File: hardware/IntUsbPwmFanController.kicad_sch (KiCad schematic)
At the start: 53 parts, among them J1 UsbPortA, J2 UsbPortB, J3 MOLEX, J6 FAN, J7 USB_Out, J8 GPIO, Q1 IRLML6402, U1 FT260S, U2 AT24CS01-SSHM, U3 ATtiny202-SS

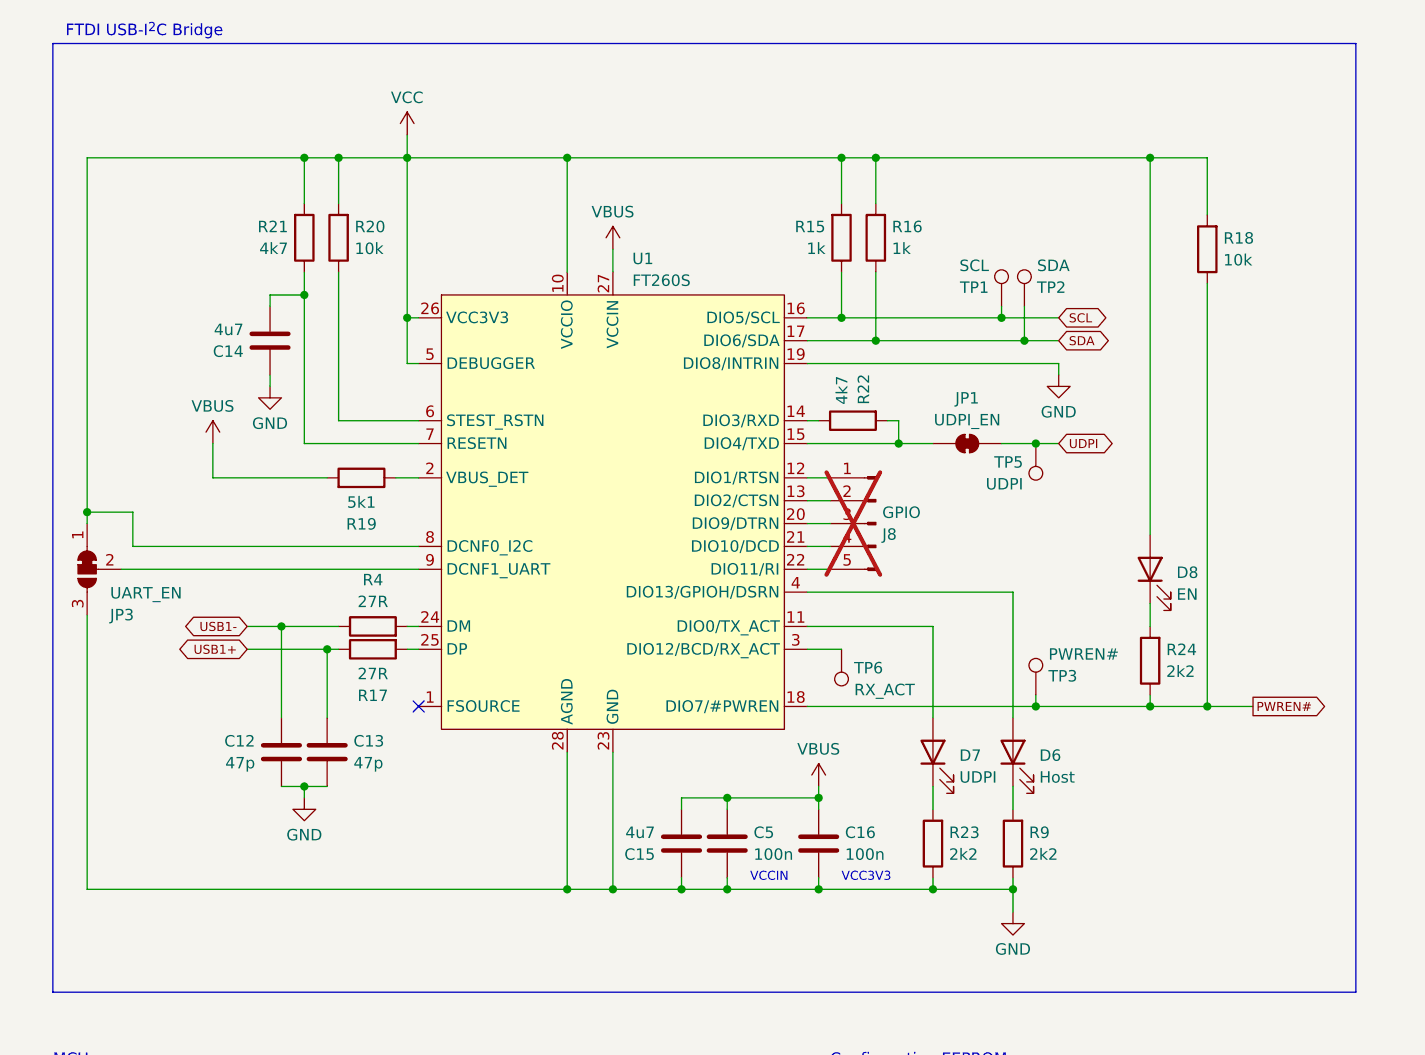
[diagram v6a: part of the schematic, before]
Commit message: Fix FT260S decoupling cap assignment
C16 was accidentally assigned to vbus, when it should have been VCC3V3.
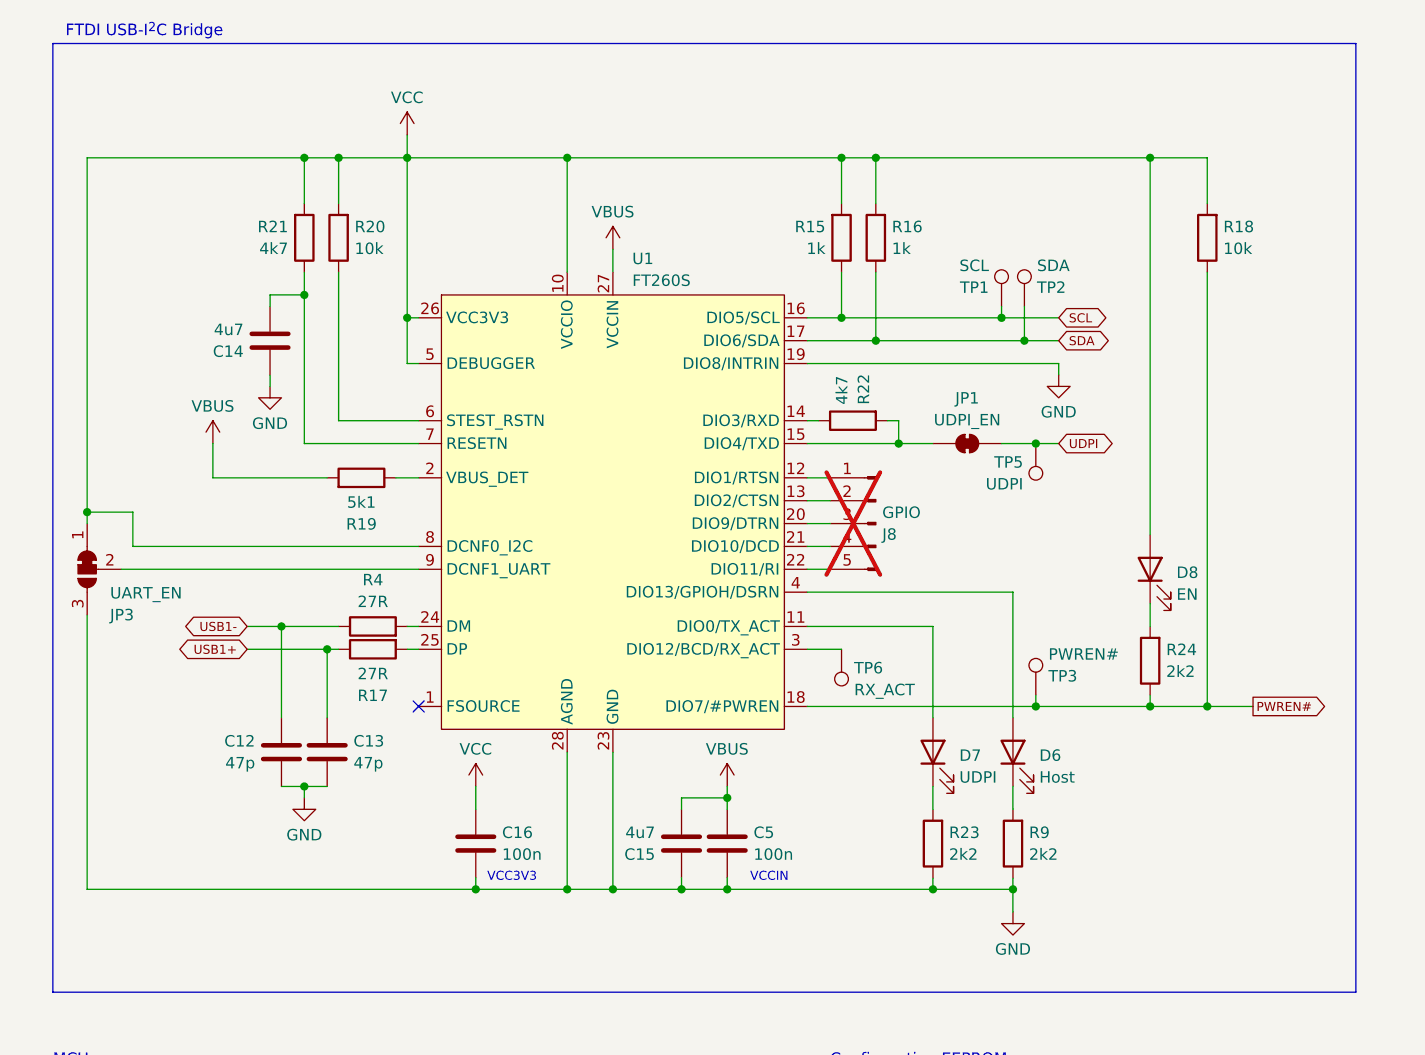
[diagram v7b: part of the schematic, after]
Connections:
- net VBUS: no longer C16.1
- net VCC: now also C16.1
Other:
- moved on the sheet: C16, R18
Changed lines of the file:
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@@
 	(text "VCC3V3"
 		(exclude_from_sim no)
-		(at 106.68 110.49 0)
+		(at 67.31 110.49 0)
 		(effects
 			(font
@@
 	)
 	(junction
+		(at 66.04 111.76)
+		(diameter 0)
+		(color 0 0 0 0)
+	)
+	(junction
 		(at 93.98 101.6)
 		(diameter 0)
@@
 	)
 	(junction
-		(at 104.14 111.76)
-		(diameter 0)
-		(color 0 0 0 0)
-	)
-	(junction
 		(at 212.09 96.52)
 		(diameter 0)
@@
 	)
 	(junction
-		(at 104.14 101.6)
-		(diameter 0)
-		(color 0 0 0 0)
-	)
-	(junction
 		(at 196.85 96.52)
 		(diameter 0)
@@
 	(wire
 		(pts
-			(xy 147.32 30.48) (xy 147.32 36.83)
+			(xy 147.32 30.48) (xy 147.32 35.56)
 		)
 		(stroke
@@
 	(wire
 		(pts
+			(xy 66.04 111.76) (xy 76.2 111.76)
+		)
+		(stroke
+			(width 0)
+			(type default)
+		)
+	)
+	(wire
+		(pts
 			(xy 135.89 160.02) (xy 135.89 161.29)
 		)
@@
 	(wire
 		(pts
+			(xy 88.9 111.76) (xy 93.98 111.76)
+		)
+		(stroke
+			(width 0)
+			(type default)
+		)
+	)
+	(wire
+		(pts
 			(xy 46.99 30.48) (xy 50.8 30.48)
 		)
@@
 	(wire
 		(pts
-			(xy 104.14 110.49) (xy 104.14 111.76)
+			(xy 66.04 110.49) (xy 66.04 111.76)
 		)
 		(stroke
@@
 	(wire
 		(pts
-			(xy 125.73 149.86) (xy 124.46 149.86)
+			(xy 93.98 100.33) (xy 93.98 101.6)
 		)
 		(stroke
@@
 	(wire
 		(pts
-			(xy 237.49 74.93) (xy 238.76 74.93)
+			(xy 125.73 149.86) (xy 124.46 149.86)
 		)
 		(stroke
@@
 	(wire
 		(pts
-			(xy 93.98 111.76) (xy 104.14 111.76)
+			(xy 237.49 74.93) (xy 238.76 74.93)
 		)
 		(stroke
@@
 	(wire
 		(pts
-			(xy 88.9 111.76) (xy 93.98 111.76)
-		)
-		(stroke
-			(width 0)
-			(type default)
-		)
-	)
-	(wire
-		(pts
 			(xy 124.46 62.23) (xy 128.27 62.23)
 		)
@@
 	(wire
 		(pts
-			(xy 147.32 44.45) (xy 147.32 91.44)
+			(xy 147.32 43.18) (xy 147.32 91.44)
 		)
 		(stroke
@@
 	(wire
 		(pts
-			(xy 104.14 100.33) (xy 104.14 101.6)
-		)
-		(stroke
-			(width 0)
-			(type default)
-		)
-	)
-	(wire
-		(pts
-			(xy 93.98 101.6) (xy 104.14 101.6)
-		)
-		(stroke
-			(width 0)
-			(type default)
-		)
-	)
-	(wire
-		(pts
 			(xy 201.93 40.64) (xy 198.12 40.64)
 		)
@@
 	(wire
 		(pts
-			(xy 104.14 111.76) (xy 116.84 111.76)
-		)
-		(stroke
-			(width 0)
-			(type default)
-		)
-	)
-	(wire
-		(pts
 			(xy 102.87 53.34) (xy 130.81 53.34)
 		)
@@
 	(wire
 		(pts
-			(xy 22.86 111.76) (xy 76.2 111.76)
+			(xy 22.86 111.76) (xy 66.04 111.76)
 		)
 		(stroke
@@
 	(wire
 		(pts
-			(xy 104.14 101.6) (xy 104.14 102.87)
+			(xy 66.04 100.33) (xy 66.04 102.87)
 		)
 		(stroke
@@
 	(wire
 		(pts
+			(xy 93.98 111.76) (xy 116.84 111.76)
+		)
+		(stroke
+			(width 0)
+			(type default)
+		)
+	)
+	(wire
+		(pts
 			(xy 228.6 96.52) (xy 228.6 99.06)
 		)
@@
 	(symbol
 		(lib_id "Device:C")
-		(at 104.14 106.68 0)
+		(at 66.04 106.68 0)
 		(unit 1)
 		(exclude_from_sim no)
@@
 		(dnp no)
 		(property "Reference" "C16"
-			(at 107.061 105.4678 0)
+			(at 68.961 105.4678 0)
 			(effects
 				(font
@@
 		)
 		(property "Value" "100n"
-			(at 107.061 107.8921 0)
+			(at 68.961 107.8921 0)
 			(effects
 				(font
@@
 		)
 		(property "Footprint" "Capacitor_SMD:C_0603_1608Metric_Pad1.08x0.95mm_HandSolder"
-			(at 105.1052 110.49 0)
+			(at 67.0052 110.49 0)
 			(effects
 				(font
@@
 		)
 		(property "Datasheet" "~"
-			(at 104.14 106.68 0)
+			(at 66.04 106.68 0)
 			(effects
 				(font
@@
 		)
 		(property "Description" "Unpolarized capacitor"
-			(at 104.14 106.68 0)
+			(at 66.04 106.68 0)
 			(effects
 				(font
@@
 		)
 		(property "Mouser No" "963-TMK107BJ104MA-T"
-			(at 109.22 110.49 0)
+			(at 71.12 110.49 0)
 			(effects
 				(font
@@
 	(symbol
 		(lib_id "power:VCC")
+		(at 66.04 100.33 0)
+		(unit 1)
+		(exclude_from_sim no)
+		(in_bom yes)
+		(on_board yes)
+		(dnp no)
+		(fields_autoplaced yes)
+		(property "Reference" "#PWR016"
+			(at 66.04 104.14 0)
+			(effects
+				(font
+					(size 1.27 1.27)
+				)
+				(hide yes)
+			)
+		)
+		(property "Value" "VCC"
+			(at 66.04 96.1969 0)
+			(effects
+				(font
+					(size 1.27 1.27)
+				)
+			)
+		)
+		(property "Footprint" ""
+			(at 66.04 100.33 0)
+			(effects
+				(font
+					(size 1.27 1.27)
+				)
+				(hide yes)
+			)
+		)
+		(property "Datasheet" ""
+			(at 66.04 100.33 0)
+			(effects
+				(font
+					(size 1.27 1.27)
+				)
+				(hide yes)
+			)
+		)
+		(property "Description" "Power symbol creates a global label with name \"VCC\""
+			(at 66.04 100.33 0)
+			(effects
+				(font
+					(size 1.27 1.27)
+				)
+				(hide yes)
+			)
+		)
+		(pin "1"
+		)
+		(instances
+			(project "IntUsbPwmFanController"
+				(path "/0a081858-7105-499c-8ae3-353b1745699c"
+					(reference "#PWR016")
+					(unit 1)
+				)
+			)
+		)
+	)
+	(symbol
+		(lib_id "power:VCC")
 		(at 135.89 142.24 0)
 		(unit 1)
@@
 	(symbol
 		(lib_id "Device:R")
-		(at 147.32 40.64 180)
+		(at 147.32 39.37 180)
 		(unit 1)
 		(exclude_from_sim no)
@@
 		(fields_autoplaced yes)
 		(property "Reference" "R18"
-			(at 149.098 39.4278 0)
+			(at 149.098 38.1578 0)
 			(effects
 				(font
@@
 		)
 		(property "Value" "10k"
-			(at 149.098 41.8521 0)
+			(at 149.098 40.5821 0)
 			(effects
 				(font
@@
 		)
 		(property "Footprint" "Resistor_SMD:R_0603_1608Metric_Pad0.98x0.95mm_HandSolder"
-			(at 149.098 40.64 90)
+			(at 149.098 39.37 90)
 			(effects
 				(font
@@
 		)
 		(property "Datasheet" "~"
-			(at 147.32 40.64 0)
+			(at 147.32 39.37 0)
 			(effects
 				(font
@@
 		)
 		(property "Description" "Resistor"
-			(at 147.32 40.64 0)
+			(at 147.32 39.37 0)
 			(effects
 				(font
@@
 	(symbol
 		(lib_id "power:VBUS")
-		(at 104.14 100.33 0)
+		(at 93.98 100.33 0)
 		(unit 1)
 		(exclude_from_sim no)
@@
 		(dnp no)
 		(property "Reference" "#PWR019"
-			(at 104.14 104.14 0)
+			(at 93.98 104.14 0)
 			(effects
 				(font
@@
 		)
 		(property "Value" "VBUS"
-			(at 104.14 96.1969 0)
+			(at 93.98 96.1969 0)
 			(effects
 				(font
@@
 		)
 		(property "Footprint" ""
-			(at 104.14 100.33 0)
+			(at 93.98 100.33 0)
 			(effects
 				(font
@@
 		)
 		(property "Datasheet" ""
-			(at 104.14 100.33 0)
+			(at 93.98 100.33 0)
 			(effects
 				(font
@@
 		)
 		(property "Description" "Power symbol creates a global label with name \"VBUS\""
-			(at 104.14 100.33 0)
+			(at 93.98 100.33 0)
 			(effects
 				(font

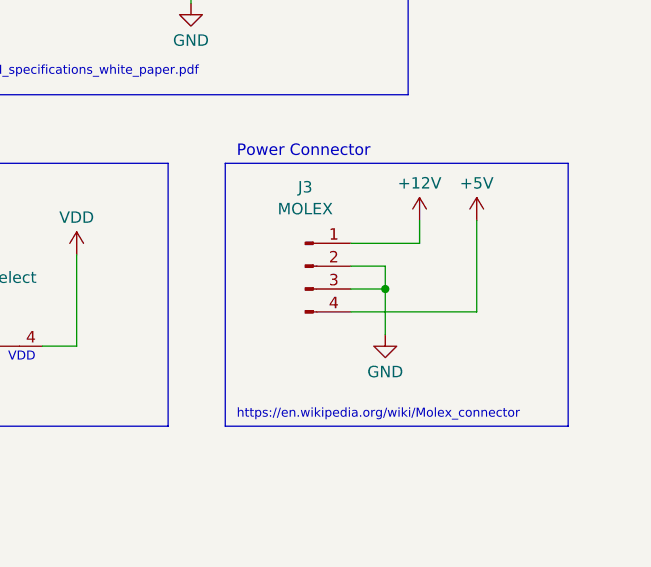
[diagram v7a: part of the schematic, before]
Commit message: Use the correct Molex connector symbol/footprint
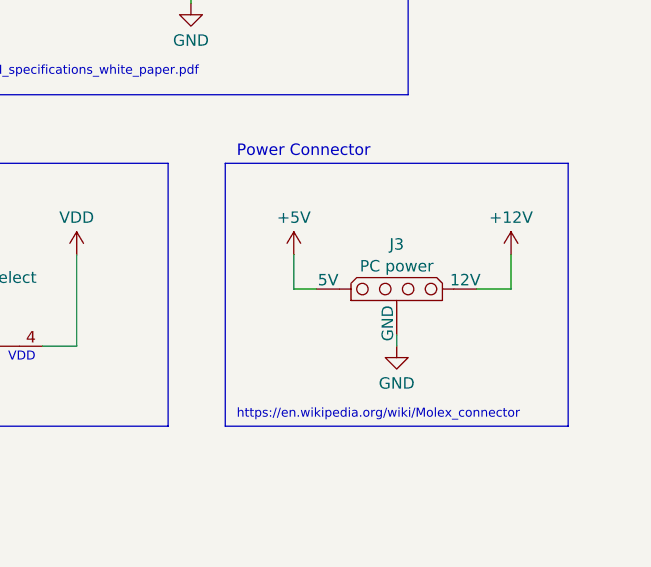
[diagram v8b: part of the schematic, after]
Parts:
- J3: value MOLEX -> PC power; footprint (none) -> Molex:Molex 8981 Vertical; symbol Connector:Conn_01x04_Pin -> Molex:Connector-Molex-8981
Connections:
- net GND: now also J3.23 (GND); no longer J3.2 (Pin_2), J3.3 (Pin_3)
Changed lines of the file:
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@@
 	)
 	(junction
-		(at 260.35 146.05)
-		(diameter 0)
-		(color 0 0 0 0)
-	)
-	(junction
 		(at 233.68 99.06)
 		(diameter 0)
@@
 	(wire
 		(pts
-			(xy 264.16 140.97) (xy 264.16 138.43)
-		)
-		(stroke
-			(width 0)
-			(type default)
-		)
-	)
-	(wire
-		(pts
 			(xy 128.27 91.44) (xy 140.97 91.44)
 		)
@@
 	(wire
 		(pts
-			(xy 147.32 161.29) (xy 135.89 161.29)
+			(xy 250.19 142.24) (xy 250.19 146.05)
 		)
 		(stroke
@@
 	(wire
 		(pts
-			(xy 146.05 152.4) (xy 151.13 152.4)
+			(xy 147.32 161.29) (xy 135.89 161.29)
 		)
 		(stroke
@@
 	(wire
 		(pts
-			(xy 125.73 110.49) (xy 125.73 111.76)
+			(xy 146.05 152.4) (xy 151.13 152.4)
 		)
 		(stroke
@@
 	(wire
 		(pts
-			(xy 111.76 59.69) (xy 113.03 59.69)
+			(xy 125.73 110.49) (xy 125.73 111.76)
 		)
 		(stroke
@@
 	(wire
 		(pts
-			(xy 256.54 143.51) (xy 260.35 143.51)
+			(xy 111.76 59.69) (xy 113.03 59.69)
 		)
 		(stroke
@@
 	(wire
 		(pts
-			(xy 237.49 74.93) (xy 238.76 74.93)
+			(xy 261.62 151.13) (xy 261.62 152.4)
 		)
 		(stroke
@@
 	(wire
 		(pts
-			(xy 256.54 140.97) (xy 264.16 140.97)
+			(xy 237.49 74.93) (xy 238.76 74.93)
 		)
 		(stroke
@@
 	(wire
 		(pts
-			(xy 270.51 148.59) (xy 270.51 138.43)
-		)
-		(stroke
-			(width 0)
-			(type default)
-		)
-	)
-	(wire
-		(pts
 			(xy 124.46 152.4) (xy 124.46 154.94)
 		)
@@
 	(wire
 		(pts
-			(xy 124.46 62.23) (xy 128.27 62.23)
+			(xy 274.32 146.05) (xy 270.51 146.05)
 		)
 		(stroke
@@
 	(wire
 		(pts
-			(xy 50.8 59.69) (xy 50.8 43.18)
+			(xy 124.46 62.23) (xy 128.27 62.23)
 		)
 		(stroke
@@
 	(wire
 		(pts
-			(xy 140.97 80.01) (xy 140.97 82.55)
+			(xy 50.8 59.69) (xy 50.8 43.18)
 		)
 		(stroke
@@
 	(wire
 		(pts
-			(xy 260.35 146.05) (xy 260.35 151.13)
+			(xy 140.97 80.01) (xy 140.97 82.55)
 		)
 		(stroke
@@
 	(wire
 		(pts
-			(xy 256.54 148.59) (xy 270.51 148.59)
+			(xy 233.68 43.18) (xy 222.25 43.18)
 		)
 		(stroke
@@
 	(wire
 		(pts
-			(xy 233.68 43.18) (xy 222.25 43.18)
+			(xy 274.32 142.24) (xy 274.32 146.05)
 		)
 		(stroke
@@
 	(wire
 		(pts
-			(xy 260.35 143.51) (xy 260.35 146.05)
-		)
-		(stroke
-			(width 0)
-			(type default)
-		)
-	)
-	(wire
-		(pts
 			(xy 80.01 139.7) (xy 80.01 142.24)
 		)
@@
 	(wire
 		(pts
-			(xy 196.85 86.36) (xy 196.85 96.52)
+			(xy 250.19 146.05) (xy 252.73 146.05)
 		)
 		(stroke
@@
 	(wire
 		(pts
-			(xy 212.09 100.33) (xy 212.09 96.52)
+			(xy 196.85 86.36) (xy 196.85 96.52)
 		)
 		(stroke
@@
 	(wire
 		(pts
-			(xy 201.93 40.64) (xy 198.12 40.64)
+			(xy 212.09 100.33) (xy 212.09 96.52)
 		)
 		(stroke
@@
 	(wire
 		(pts
-			(xy 256.54 146.05) (xy 260.35 146.05)
+			(xy 201.93 40.64) (xy 198.12 40.64)
 		)
 		(stroke
@@
 	(symbol
 		(lib_id "power:+12V")
-		(at 264.16 138.43 0)
+		(at 274.32 142.24 0)
 		(unit 1)
 		(exclude_from_sim no)
@@
 		(fields_autoplaced yes)
 		(property "Reference" "#PWR06"
-			(at 264.16 142.24 0)
+			(at 274.32 146.05 0)
 			(effects
 				(font
@@
 		)
 		(property "Value" "+12V"
-			(at 264.16 134.2969 0)
+			(at 274.32 138.1069 0)
 			(effects
 				(font
@@
 		)
 		(property "Footprint" ""
-			(at 264.16 138.43 0)
+			(at 274.32 142.24 0)
 			(effects
 				(font
@@
 		)
 		(property "Datasheet" ""
-			(at 264.16 138.43 0)
+			(at 274.32 142.24 0)
 			(effects
 				(font
@@
 		)
 		(property "Description" "Power symbol creates a global label with name \"+12V\""
-			(at 264.16 138.43 0)
+			(at 274.32 142.24 0)
 			(effects
 				(font
@@
 	(symbol
 		(lib_id "power:+5V")
-		(at 270.51 138.43 0)
+		(at 250.19 142.24 0)
 		(unit 1)
 		(exclude_from_sim no)
@@
 		(fields_autoplaced yes)
 		(property "Reference" "#PWR07"
-			(at 270.51 142.24 0)
+			(at 250.19 146.05 0)
 			(effects
 				(font
@@
 		)
 		(property "Value" "+5V"
-			(at 270.51 134.2969 0)
+			(at 250.19 138.1069 0)
 			(effects
 				(font
@@
 		)
 		(property "Footprint" ""
-			(at 270.51 138.43 0)
+			(at 250.19 142.24 0)
 			(effects
 				(font
@@
 		)
 		(property "Datasheet" ""
-			(at 270.51 138.43 0)
+			(at 250.19 142.24 0)
 			(effects
 				(font
@@
 		)
 		(property "Description" "Power symbol creates a global label with name \"+5V\""
-			(at 270.51 138.43 0)
+			(at 250.19 142.24 0)
 			(effects
 				(font
@@
 	(symbol
 		(lib_id "power:GND")
-		(at 260.35 151.13 0)
+		(at 261.62 152.4 0)
 		(unit 1)
 		(exclude_from_sim no)
@@
 		(fields_autoplaced yes)
 		(property "Reference" "#PWR08"
-			(at 260.35 157.48 0)
+			(at 261.62 158.75 0)
 			(effects
 				(font
@@
 		)
 		(property "Value" "GND"
-			(at 260.35 155.2631 0)
+			(at 261.62 156.5331 0)
 			(effects
 				(font
@@
 		)
 		(property "Footprint" ""
-			(at 260.35 151.13 0)
+			(at 261.62 152.4 0)
 			(effects
 				(font
@@
 		)
 		(property "Datasheet" ""
-			(at 260.35 151.13 0)
+			(at 261.62 152.4 0)
 			(effects
 				(font
@@
 		)
 		(property "Description" "Power symbol creates a global label with name \"GND\" , ground"
-			(at 260.35 151.13 0)
+			(at 261.62 152.4 0)
 			(effects
 				(font
@@
 	)
 	(symbol
-		(lib_id "Connector:Conn_01x04_Pin")
-		(at 251.46 143.51 0)
+		(lib_id "Molex:Connector-Molex-8981")
+		(at 261.62 146.05 0)
 		(unit 1)
 		(exclude_from_sim no)
@@
 		(dnp no)
 		(property "Reference" "J3"
-			(at 251.46 134.7357 0)
+			(at 261.62 141.0857 0)
 			(effects
 				(font
@@
 			)
 		)
-		(property "Value" "MOLEX"
-			(at 251.46 137.16 0)
+		(property "Value" "PC power"
+			(at 261.62 143.51 0)
 			(effects
 				(font
@@
 			)
 		)
-		(property "Footprint" ""
-			(at 251.46 143.51 0)
+		(property "Footprint" "Molex:Molex 8981 Vertical"
+			(at 261.62 146.05 0)
 			(effects
 				(font
@@
 			)
 		)
-		(property "Datasheet" "~"
-			(at 251.46 143.51 0)
+		(property "Datasheet" "https://en.wikipedia.org/wiki/Molex_connector"
+			(at 261.366 162.306 0)
 			(effects
 				(font
@@
 			)
 		)
-		(property "Description" "Generic connector, single row, 01x04, script generated"
-			(at 251.46 143.51 0)
+		(property "Description" "Molex 8981 board-side connector (Hard Drive power connector)"
+			(at 261.874 159.766 0)
 			(effects
 				(font
@@
 		(pin "1"
 		)
-		(pin "2"
+		(pin "23"
 		)
 		(pin "4"
 		)
-		(pin "3"
-		)
 		(instances
